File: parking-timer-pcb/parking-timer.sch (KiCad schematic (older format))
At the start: 1 part, among them U1 RDA5807M

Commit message: Printed FM antenna design, castellation footprint for RDA5807M, RF filter.
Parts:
- added AE1: Antenna, parking-timer-pcb:FM-printed-antenna, symbol Device:Antenna
- added C1: 82pF, Capacitor_SMD:C_0805_2012Metric, symbol Device:C
- added C2: 68pF, Capacitor_SMD:C_0805_2012Metric, symbol Device:C
- added L1: 1.5nH, Inductor_SMD:L_0805_2012Metric, symbol Device:L
- added L2: 100nH, Inductor_SMD:L_0805_2012Metric, symbol Device:L
- added L3: 68nH, Inductor_SMD:L_0805_2012Metric, symbol Device:L
- U1: footprint parking-timer-pcb:RDA5807M-sunken -> parking-timer-pcb:RDA5807M-through-hole
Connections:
- wire segments 0 -> 10
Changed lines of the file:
@@
 EESchema Schematic File Version 4
+LIBS:parking-timer-cache
 EELAYER 26 0
 EELAYER END
@@
 F 0 "U1" H 8800 3715 50  0000 C CNN
 F 1 "RDA5807M" H 8800 3624 50  0000 C CNN
-F 2 "parking-timer-pcb:RDA5807M-sunken" H 8800 3350 50  0001 C CNN
+F 2 "parking-timer-pcb:RDA5807M-through-hole" H 8800 3350 50  0001 C CNN
 F 3 "" H 8800 3350 50  0001 C CNN
 	1    8800 3250
 	1    0    0    -1
 $EndComp
+$Comp
+L Device:Antenna AE1
+U 1 1 5FA7C4B6
+P 9550 1850
+F 0 "AE1" H 9630 1841 50  0000 L CNN
+F 1 "Antenna" H 9630 1750 50  0000 L CNN
+F 2 "parking-timer-pcb:FM-printed-antenna" H 9550 1850 50  0001 C CNN
+F 3 "~" H 9550 1850 50  0001 C CNN
+	1    9550 1850
+	1    0    0    -1
+$EndComp
+$Comp
+L Device:C C2
+U 1 1 5FA7D28D
+P 9950 2950
+F 0 "C2" V 9698 2950 50  0000 C CNN
+F 1 "68pF" V 9789 2950 50  0000 C CNN
+F 2 "Capacitor_SMD:C_0805_2012Metric" H 9988 2800 50  0001 C CNN
+F 3 "~" H 9950 2950 50  0001 C CNN
+	1    9950 2950
+	0    1    1    0
+$EndComp
+$Comp
+L Device:C C1
+U 1 1 5FA7D338
+P 9950 2550
+F 0 "C1" V 9698 2550 50  0000 C CNN
+F 1 "82pF" V 9789 2550 50  0000 C CNN
+F 2 "Capacitor_SMD:C_0805_2012Metric" H 9988 2400 50  0001 C CNN
+F 3 "~" H 9950 2550 50  0001 C CNN
+	1    9950 2550
+	0    1    1    0
+$EndComp
+$Comp
+L Device:L L2
+U 1 1 5FA7D3B3
+P 9550 2750
+F 0 "L2" H 9603 2796 50  0000 L CNN
+F 1 "100nH" H 9603 2705 50  0000 L CNN
+F 2 "Inductor_SMD:L_0805_2012Metric" H 9550 2750 50  0001 C CNN
+F 3 "~" H 9550 2750 50  0001 C CNN
+	1    9550 2750
+	1    0    0    -1
+$EndComp
+$Comp
+L Device:L L1
+U 1 1 5FA7D447
+P 9550 2350
+F 0 "L1" H 9603 2396 50  0000 L CNN
+F 1 "1.5nH" H 9603 2305 50  0000 L CNN
+F 2 "Inductor_SMD:L_0805_2012Metric" H 9550 2350 50  0001 C CNN
+F 3 "~" H 9550 2350 50  0001 C CNN
+	1    9550 2350
+	1    0    0    -1
+$EndComp
+$Comp
+L Device:L L3
+U 1 1 5FA7D46F
+P 9950 2150
+F 0 "L3" V 10140 2150 50  0000 C CNN
+F 1 "68nH" V 10049 2150 50  0000 C CNN
+F 2 "Inductor_SMD:L_0805_2012Metric" H 9950 2150 50  0001 C CNN
+F 3 "~" H 9950 2150 50  0001 C CNN
+	1    9950 2150
+	0    -1   -1   0
+$EndComp
+Wire Wire Line
+	9550 2900 9550 2950
+Wire Wire Line
+	9550 3050 9400 3050
+Wire Wire Line
+	9550 2950 9800 2950
+Connection ~ 9550 2950
+Wire Wire Line
+	9550 2950 9550 3050
+Wire Wire Line
+	9800 2550 9550 2550
+Wire Wire Line
+	9550 2550 9550 2500
+Wire Wire Line
+	9550 2600 9550 2550
+Connection ~ 9550 2550
+Wire Wire Line
+	9800 2150 9550 2150
+Wire Wire Line
+	9550 2150 9550 2200
+Wire Wire Line
+	9550 2050 9550 2150
+Connection ~ 9550 2150
 $EndSCHEMATC

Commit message: Add display connector, STM8L101F3
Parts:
- removed U1: RDA5807M, parking-timer-pcb:RDA5807M-through-hole, symbol parking-timer-kicad:RDA5807M
- added C3: 100nF, Capacitor_SMD:C_0805_2012Metric, symbol Device:C
- added J1: Conn_01x02, Connector_PinHeader_2.54mm:PinHeader_1x02_P2.54mm_Vertical, symbol Connector_Generic:Conn_01x02
- added J2: Conn_02x04_Odd_Even, Connector_PinHeader_2.54mm:PinHeader_2x04_P2.54mm_Vertical, symbol Connector_Generic:Conn_02x04_Odd_Even
- added U1: RDA5807M_Module, parking-timer-pcb:RDA5807M-through-hole, symbol parking-timer-kicad:RDA5807M_Module
- added U2: STM8L101F3P, Package_SO:TSSOP-20_4.4x6.5mm_P0.65mm, symbol MCU_ST_STM8:STM8L101F3P
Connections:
- net labels added: DISP_BUSY, DISP_CS, DISP_DC, DIST_RST, GND, I2C_SDA, I2C_SDC, SPI_MOSI, SPI_SCK, UART_TX, VDD
- wire segments 10 -> 42
- no-connect marks 0 -> 2
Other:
- moved on the sheet: AE1, C1, C2, L1, L2, L3

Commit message: Parking-timer-pcb: footprint for ER-EPM029-1, LIS3DSH module. Rework placement.
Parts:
- added C4, C5: 100nF, Capacitor_SMD:C_0805_2012Metric, symbol Device:C
- added C6: 1uF, Capacitor_SMD:C_0805_2012Metric, symbol Device:C
- added J3: Conn_01x04, Connector_PinHeader_2.54mm:PinHeader_1x04_P2.54mm_Vertical, symbol Connector_Generic:Conn_01x04
- added J4: Conn_01x11, parking-timer-pcb:LIS3DSH_Module, symbol Connector_Generic:Conn_01x11
- J2: footprint Connector_PinHeader_2.54mm:PinHeader_2x04_P2.54mm_Vertical -> parking-timer-pcb:ER-EPM029-1_Module
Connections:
- net GND: now also C4.2, C5.2, C6.2, J3.3 (Pin_3), J4.11 (Pin_11), J4.2 (Pin_2), J4.9 (Pin_9)
- net SPI_MOSI: now also J4.4 (Pin_4)
- net VDD: now also C5.1, C6.1, J3.1 (Pin_1), J4.1 (Pin_1)
- net SPI_MISO: now reaches U2.17 (PB7)
- net SPI_MISO: now also J4.5 (Pin_5)
- net SWIM: now reaches U2.3 (PA0)
- net SWIM: now also J3.2 (Pin_2)
- net NRST: now reaches J1.2 (Pin_2), U2.4 (PA1)
- net NRST: now also C4.1, J3.4 (Pin_4)
- new net ACCE_CS: J4.6 (Pin_6)
- new net ACCE_INT1: J4.7 (Pin_7)
- new net SPI_SCL: J4.3 (Pin_3)
- no-connect marks 2 -> 4
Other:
- moved on the sheet: J1

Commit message: Parking-timer-pcb: add BatteryHolder footprint, move MCU.
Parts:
- added J5: Conn_01x02, parking-timer-pcb:BatteryHolder, symbol Connector_Generic:Conn_01x02
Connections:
- net SPI_SCL is gone; now on net SPI_SCK: J4.3 (Pin_3)
- net GND: now also J5.1 (Pin_1)
- net VDD: now also J5.2 (Pin_2)
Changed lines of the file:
@@
 	2050 5450 2050 5300
 Text GLabel 2200 5650 2    50   Input ~ 0
-SPI_SCL
+SPI_SCK
 Text GLabel 2200 5750 2    50   Input ~ 0
 SPI_MOSI
@@
 Wire Wire Line
 	2050 6450 2050 6650
+$Comp
+L Connector_Generic:Conn_01x02 J5
+U 1 1 5FB16AE6
+P 1700 2250
+F 0 "J5" H 1618 1925 50  0000 C CNN
+F 1 "Conn_01x02" H 1618 2016 50  0000 C CNN
+F 2 "parking-timer-pcb:BatteryHolder" H 1700 2250 50  0001 C CNN
+F 3 "~" H 1700 2250 50  0001 C CNN
+	1    1700 2250
+	-1   0    0    1
+$EndComp
+$Comp
+L power:GND #PWR0115
+U 1 1 5FB17452
+P 2000 2350
+F 0 "#PWR0115" H 2000 2100 50  0001 C CNN
+F 1 "GND" H 2005 2177 50  0000 C CNN
+F 2 "" H 2000 2350 50  0001 C CNN
+F 3 "" H 2000 2350 50  0001 C CNN
+	1    2000 2350
+	1    0    0    -1
+$EndComp
+$Comp
+L power:VDD #PWR0116
+U 1 1 5FB17734
+P 2000 2050
+F 0 "#PWR0116" H 2000 1900 50  0001 C CNN
+F 1 "VDD" H 2015 2223 50  0000 C CNN
+F 2 "" H 2000 2050 50  0001 C CNN
+F 3 "" H 2000 2050 50  0001 C CNN
+	1    2000 2050
+	1    0    0    -1
+$EndComp
+Wire Wire Line
+	1900 2150 2000 2150
+Wire Wire Line
+	2000 2150 2000 2050
+Wire Wire Line
+	1900 2250 2000 2250
+Wire Wire Line
+	2000 2250 2000 2350
 $EndSCHEMATC

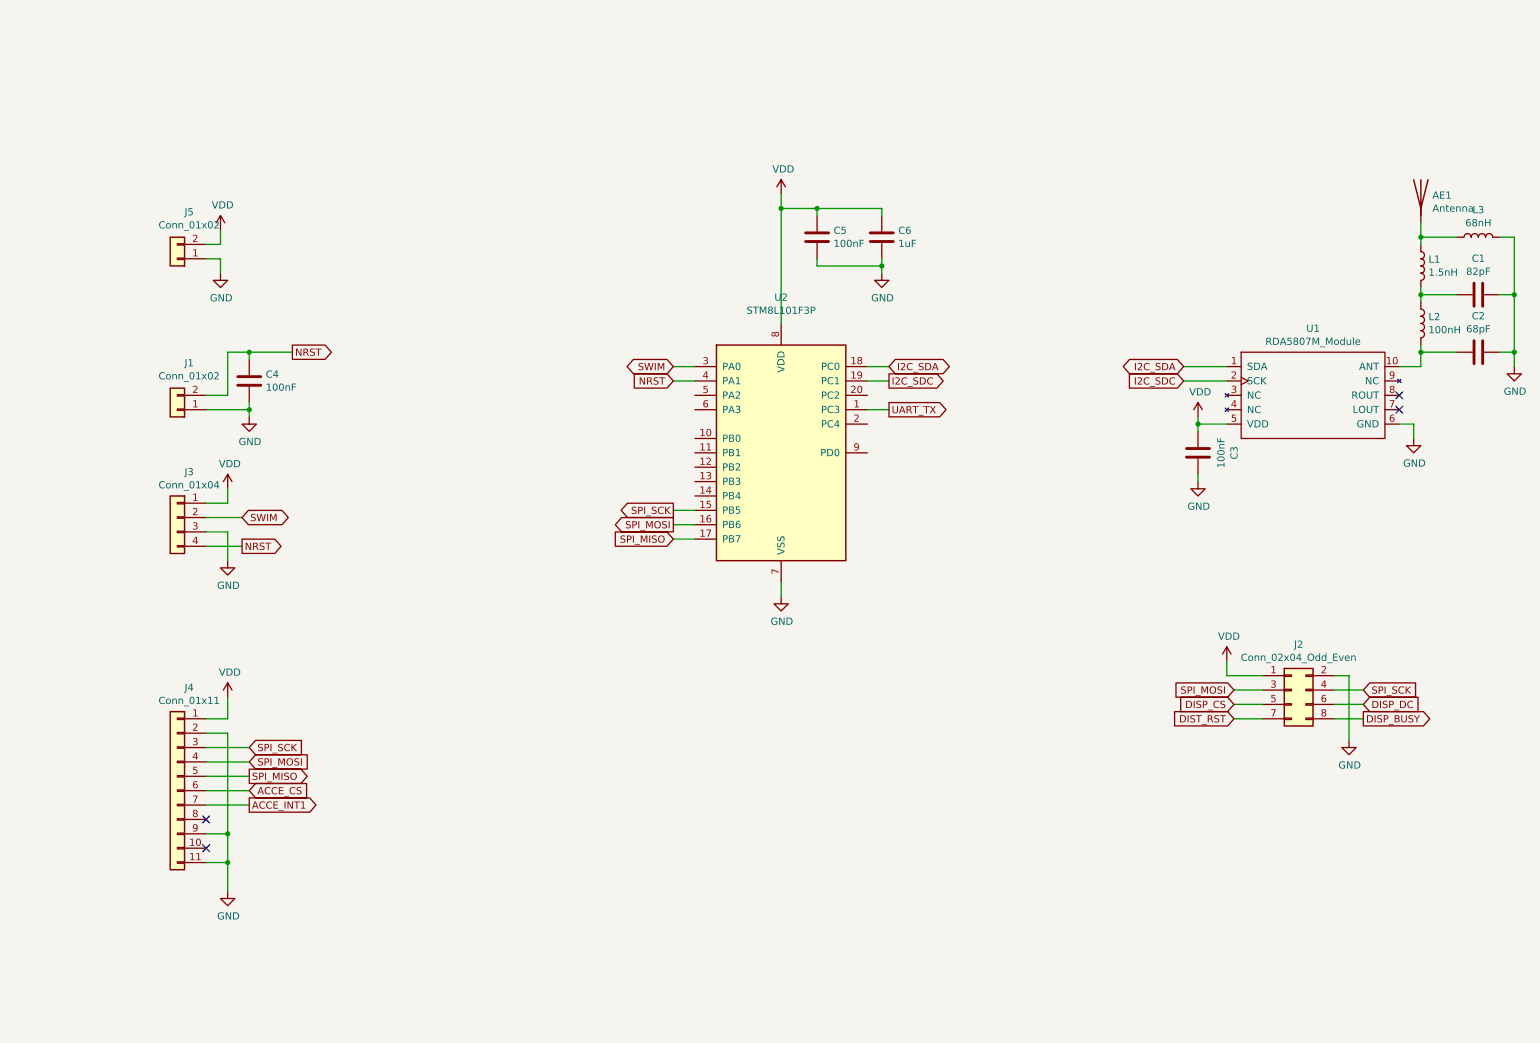
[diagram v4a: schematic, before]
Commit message: Parking-timer-pcb: Fix ER-EPM029 footprint holes, add ADS1220 and a bazillion of other layout changes.
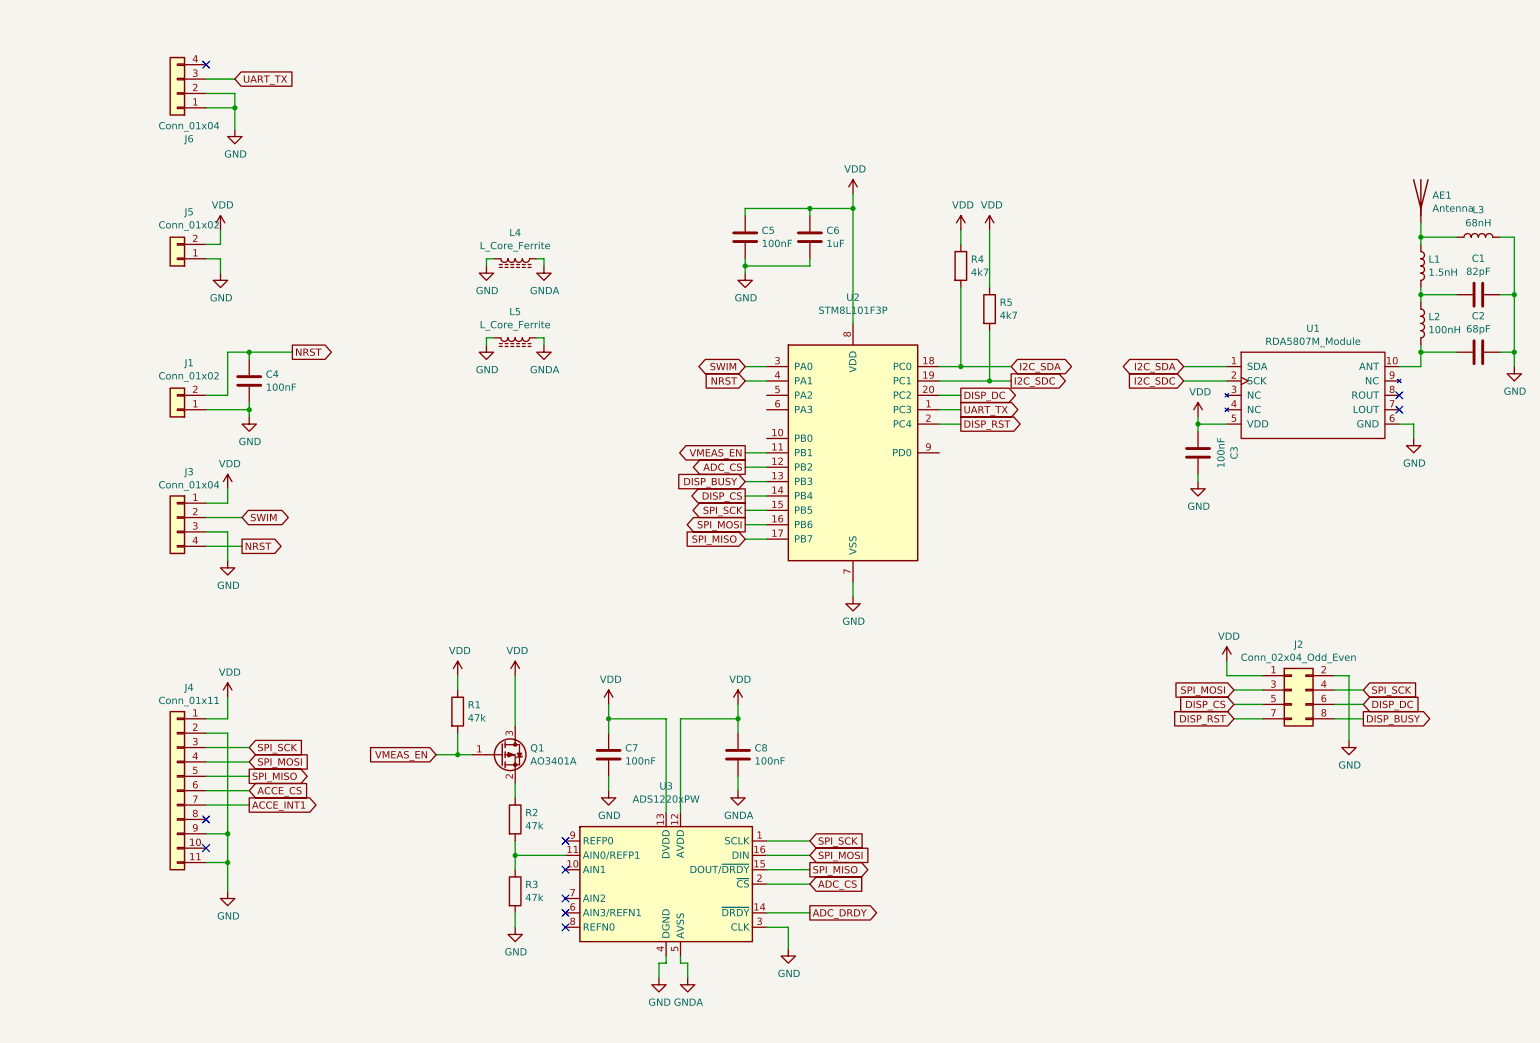
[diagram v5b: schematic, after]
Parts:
- added C7, C8: 100nF, Capacitor_SMD:C_0805_2012Metric, symbol Device:C
- added J6: Conn_01x04, Connector_PinHeader_2.54mm:PinHeader_1x04_P2.54mm_Vertical, symbol Connector_Generic:Conn_01x04
- added L4, L5: L_Core_Ferrite, Resistor_SMD:R_0805_2012Metric, symbol Device:L_Core_Ferrite
- added Q1: AO3401A, Package_TO_SOT_SMD:SOT-23, symbol Transistor_FET:AO3401A
- added R1, R2, R3: 47k, Resistor_SMD:R_0805_2012Metric, symbol Device:R
- added R4, R5: 4k7, Resistor_SMD:R_0805_2012Metric, symbol Device:R
- added U3: ADS1220xPW, Package_SO:TSSOP-16_4.4x5mm_P0.65mm, symbol Analog_ADC:ADS1220xPW
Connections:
- net DIST_RST is gone; now on net DISP_RST: J2.7 (Pin_7)
- net DISP_BUSY: now also U2.13 (PB3)
- net DISP_CS: now also U2.14 (PB4)
- net DISP_DC: now also U2.20 (PC2)
- net GND: now also C7.2, J6.1 (Pin_1), J6.2 (Pin_2), L4.2, L5.2, R3.2, U3.3 (CLK), U3.4 (DGND)
- net I2C_SDA: now also R4.2
- net I2C_SDC: now also R5.2
- net SPI_MISO: now also U3.15 (DOUT/~DRDY)
- net SPI_MOSI: now also U3.16 (DIN)
- net SPI_SCK: now also U3.1 (SCLK)
- net UART_TX: now also J6.3 (Pin_3)
- net VDD: now also C7.1, C8.1, Q1.3 (D), R1.1, R4.1, R5.1, U3.12 (AVDD), U3.13 (DVDD)
- net VMEAS_EN: now reaches U2.11 (PB1)
- net VMEAS_EN: now also Q1.1 (G), R1.2
- net ADC_CS: now reaches U2.12 (PB2)
- net ADC_CS: now also U3.2 (~CS)
- net DISP_RST: now reaches U2.2 (PC4)
- new net: R2.2, R3.1, U3.11 (AIN0/REFP1)
- new net: Q1.2 (S), R2.1
- new net ADC_DRDY: U3.14 (~DRDY)
- new net GNDA: C8.2, L4.1, L5.1, U3.5 (AVSS)
- no-connect marks 4 -> 10
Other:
- moved on the sheet: C5, C6, U2

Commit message: parking-timer-pcb: Add solar cell connection, update STM8L101F3 symbol and footprint from ST. Fix DRC errors.
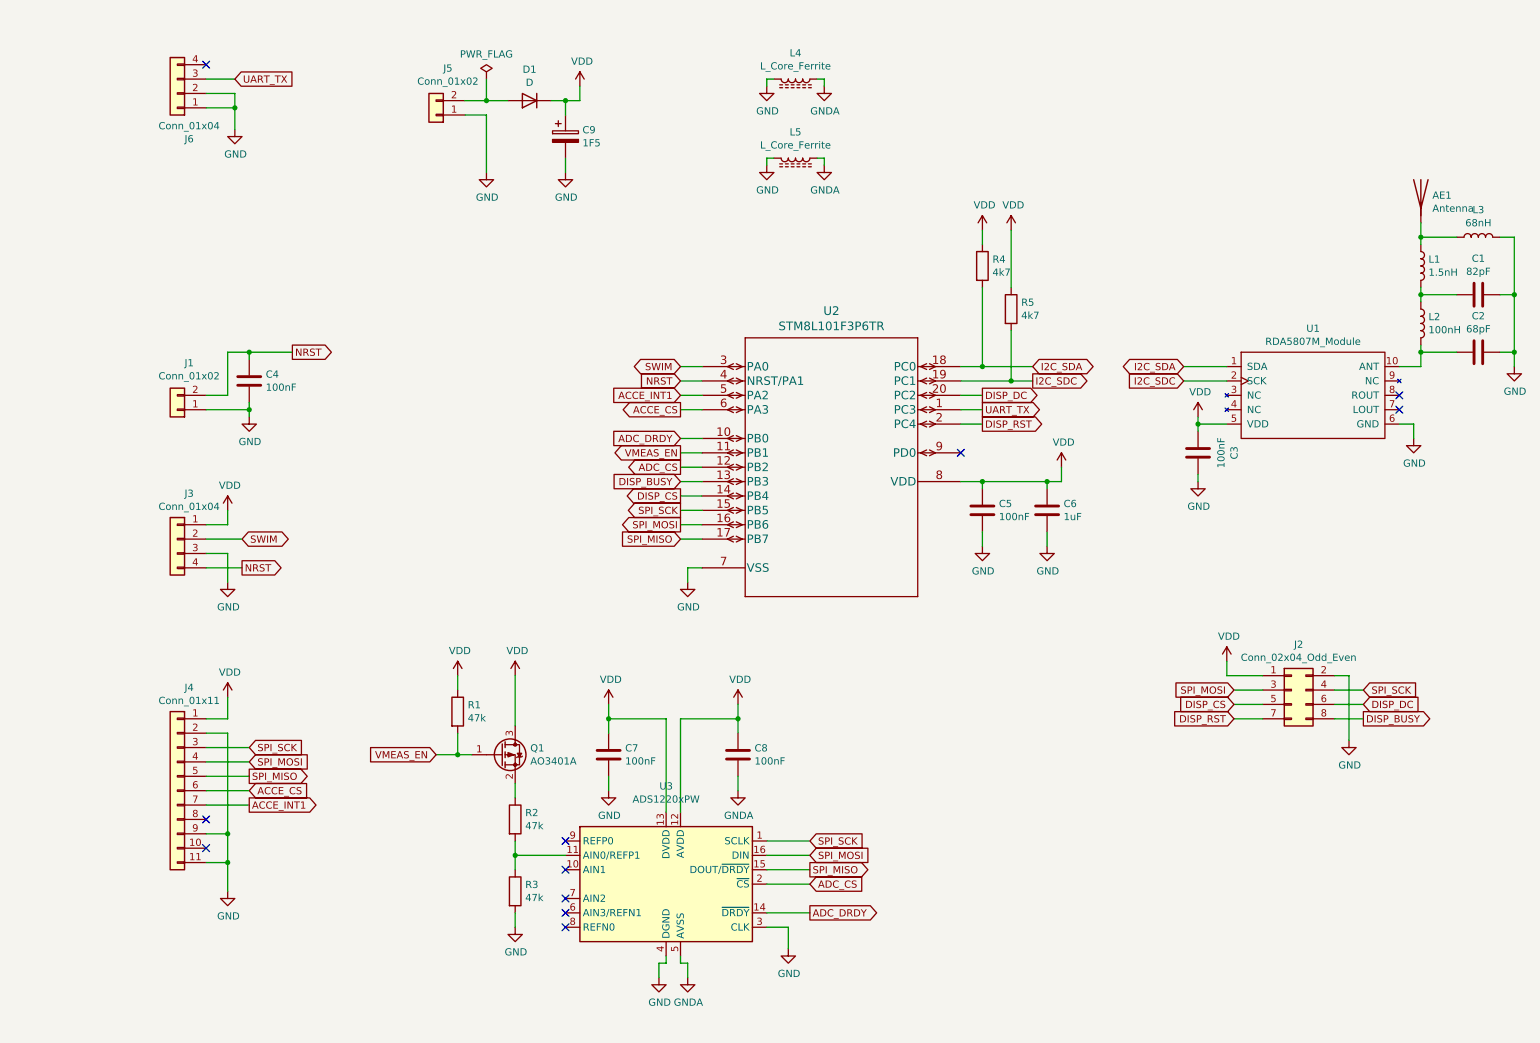
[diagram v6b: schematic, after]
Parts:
- removed U2: STM8L101F3P, Package_SO:TSSOP-20_4.4x6.5mm_P0.65mm, symbol MCU_ST_STM8:STM8L101F3P
- added C9: 1F5, parking-timer-pcb:BatteryHolder, symbol Device:CP
- added D1: D, Diode_SMD:D_0805_2012Metric_Pad1.15x1.40mm_HandSolder, symbol Device:D
- added U2: STM8L101F3P6TR, parking-timer-pcb:STM8L101F3P6TR, symbol parking-timer-kicad:STM8L101F3P6TR
- J5: footprint parking-timer-pcb:BatteryHolder -> Connector_PinHeader_2.54mm:PinHeader_1x02_P2.54mm_Vertical
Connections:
- net ACCE_CS: now also U2.6 (PA3)
- net ACCE_INT1: now also U2.5 (PA2)
- net ADC_CS: now also U2.12 (PB2)
- net ADC_DRDY: now also U2.10 (PB0)
- net DISP_BUSY: now also U2.13 (PB3)
- net DISP_CS: now also U2.14 (PB4)
- net DISP_DC: now also U2.20 (PC2)
- net DISP_RST: now also U2.2 (PC4)
- net GND: now also C9.2, U2.7 (VSS)
- net I2C_SDA: now also U2.18 (PC0)
- net I2C_SDC: now also U2.19 (PC1)
- net NRST: now also U2.4 (NRST/PA1)
- net SPI_MISO: now also U2.17 (PB7)
- net SPI_MOSI: now also U2.16 (PB6)
- net SPI_SCK: now also U2.15 (PB5)
- net SWIM: now also U2.3 (PA0)
- net UART_TX: now also U2.1 (PC3)
- net VDD: now also C9.1, D1.1 (K), U2.8 (VDD); no longer J5.2 (Pin_2)
- net VMEAS_EN: now also U2.11 (PB1)
- new net: D1.2 (A), J5.2 (Pin_2)
- no-connect marks 10 -> 11
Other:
- moved on the sheet: C5, C6, J3, L4, L5, R4, R5
